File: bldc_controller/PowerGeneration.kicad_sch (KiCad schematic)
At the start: 7 parts, among them U1 MAX15062AATA+T

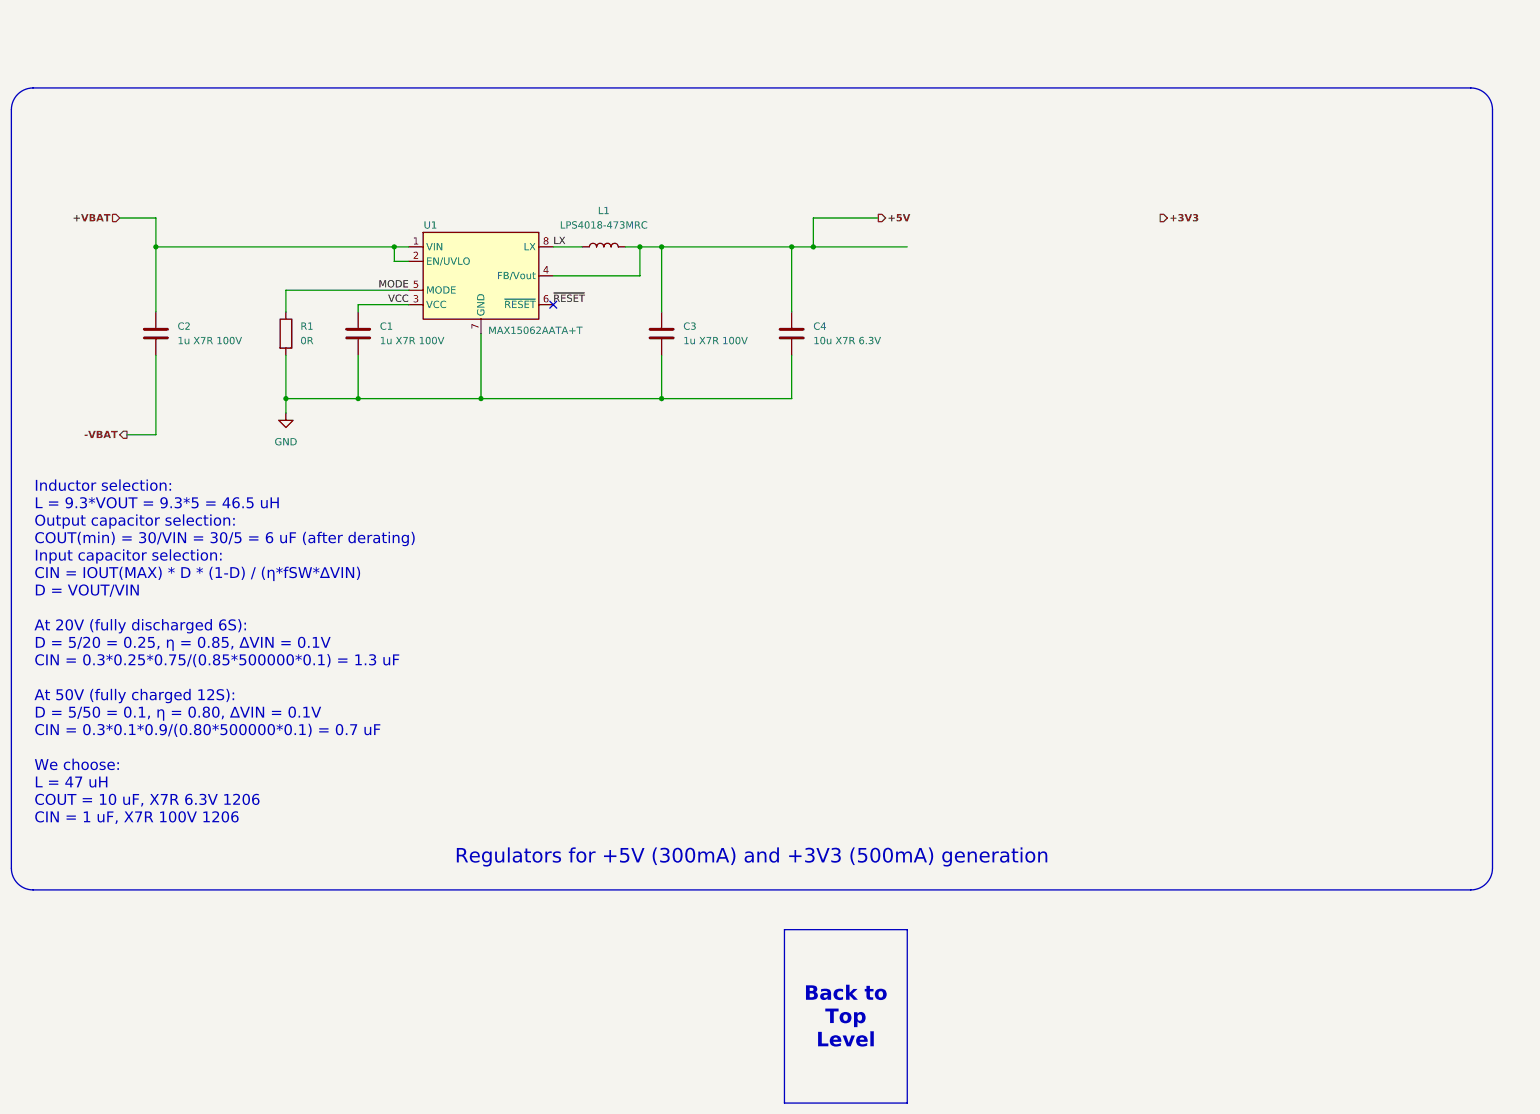
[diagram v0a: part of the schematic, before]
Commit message: added temporary footprints and deleted extra files
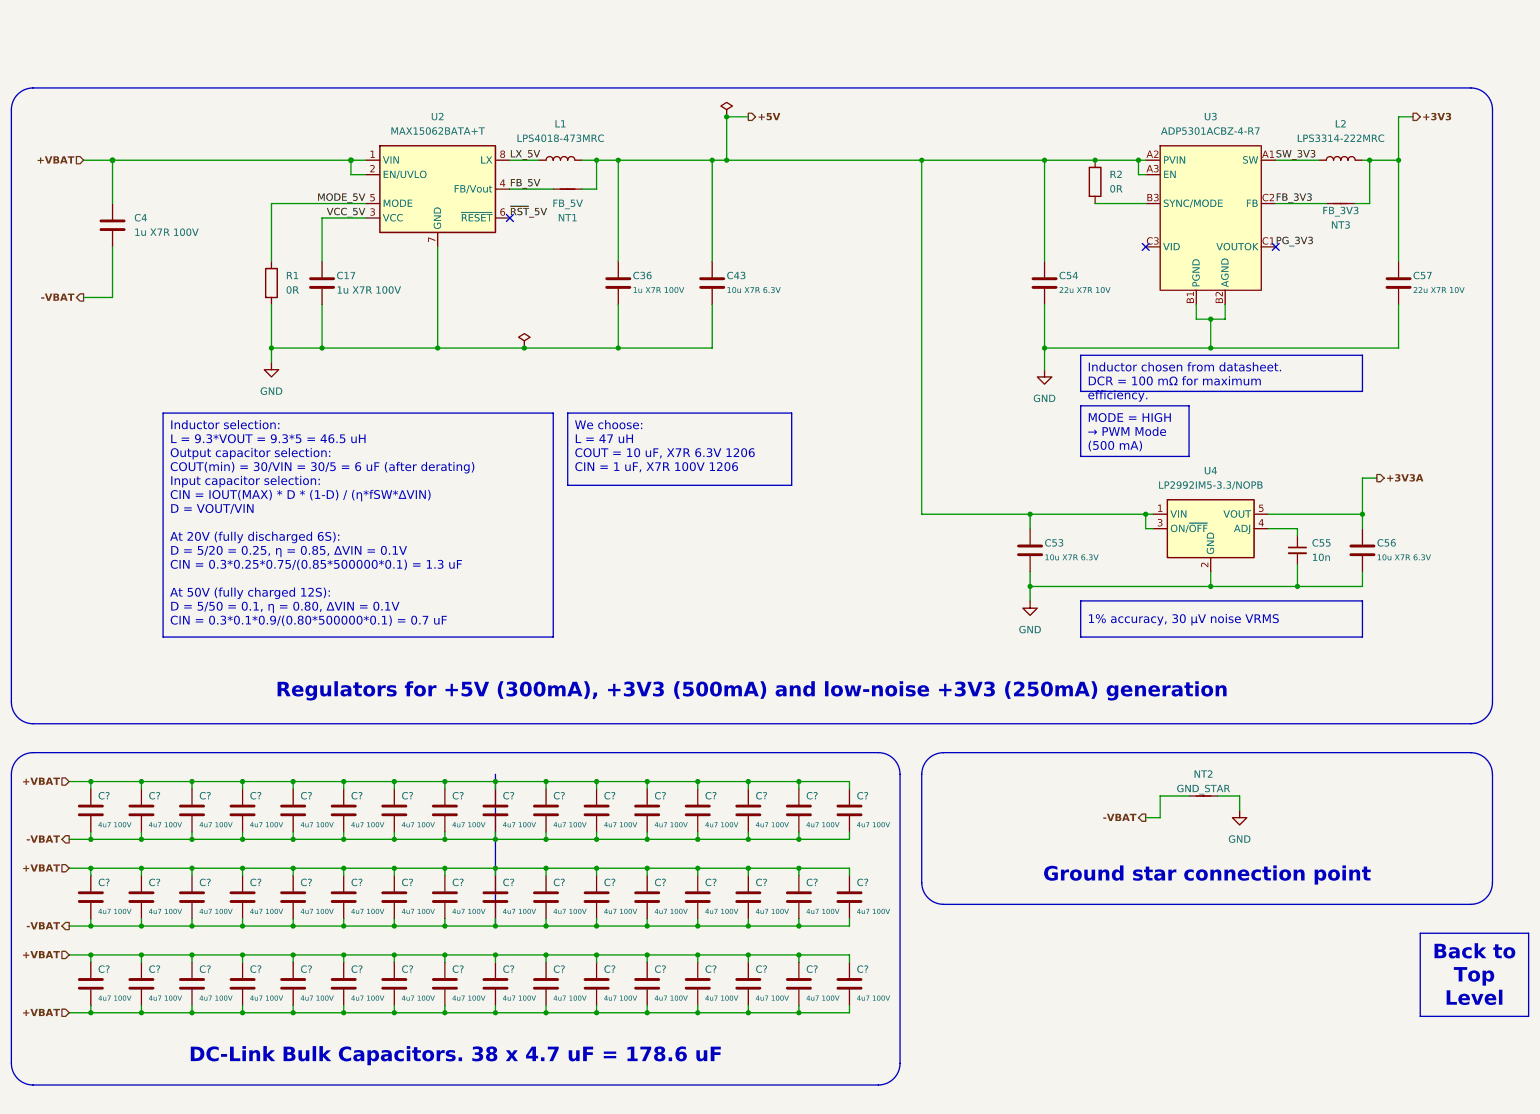
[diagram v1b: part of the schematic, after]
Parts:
- removed U1: MAX15062AATA+T, Package_DFN_QFN:DFN-8_2x2mm_P0.5mm, symbol Regulator_Switching:MAX15062A
- added C53, C56: 10u X7R 6.3V, Capacitor_SMD:C_0201_0603Metric, symbol Device:C
- added C54, C57: 22u X7R 10V, Capacitor_SMD:C_1206_3216Metric, symbol Device:C
- added C55: 10n, Capacitor_SMD:C_0402_1005Metric, symbol Device:C_Small
- added C? (x48): 4u7 100V, Capacitor_SMD:C_1206_3216Metric, symbol Device:C
- added L2: LPS3314-222MRC, Inductor_SMD:L_Coilcraft_LPS3314, symbol Device:L
- added NT1: FB_5V, NetTie:NetTie-2_SMD_Pad0.5mm, symbol Device:NetTie_2
- added NT2: GND_STAR, NetTie:NetTie-2_SMD_Pad2.0mm, symbol Device:NetTie_2
- added NT3: FB_3V3, NetTie:NetTie-2_SMD_Pad0.5mm, symbol Device:NetTie_2
- added R2: 0R, Resistor_SMD:R_0402_1005Metric, symbol Device:R
- added U2: MAX15062BATA+T, Package_DFN_QFN:DFN-8_2x2mm_P0.5mm, symbol Regulator_Switching:MAX15062B
- added U3: ADP5301ACBZ-4-R7, 0_switching_regulator:CB-9-6_ADI, symbol 0_switching_regulator:ADP5301ACBZ-4-R7
- added U4: LP2992IM5-3.3/NOPB, Package_TO_SOT_SMD:SOT-23-5, symbol 0_linear_regulator:LP2992IM5-3.3/NOPB
- C17: renamed from C1; footprint (none) -> Capacitor_SMD:C_0402_1005Metric
- C36: renamed from C3; footprint (none) -> Capacitor_SMD:C_0402_1005Metric
- C4: renamed from C2; footprint (none) -> Capacitor_SMD:C_0402_1005Metric
- C43: renamed from C4; footprint (none) -> Capacitor_SMD:C_0201_0603Metric
- R1: footprint (none) -> Resistor_SMD:R_0402_1005Metric
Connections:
- net +3V3: now also C57.1, L2.2, NT3.2
- net +5V: now also C53.1, C54.1, NT1.2, R2.1, U3.A2 (PVIN), U3.A3 (EN), U4.1 (VIN), U4.3 (ON/~{OFF})
- net +VBAT: now also C?.1, C?.1, C?.1, C?.1, C?.1, C?.1, C?.1, C?.1, C?.1, C?.1, C?.1, C?.1, C?.1, C?.1, C?.1, C?.1, C?.1, C?.1, C?.1, C?.1, C?.1, C?.1, C?.1, C?.1, C?.1, C?.1, C?.1, C?.1, C?.1, C?.1, C?.1, C?.1, C?.1, C?.1, C?.1, C?.1, C?.1, C?.1, C?.1, C?.1, C?.1, C?.1, C?.1, C?.1, C?.1, C?.1, C?.1, C?.1, C?.2, C?.2, C?.2, C?.2, C?.2, C?.2, C?.2, C?.2, C?.2, C?.2, C?.2, C?.2, C?.2, C?.2, C?.2, C?.2, U2.1 (VIN), U2.2 (EN/UVLO)
- net -VBAT: now also C?.2, C?.2, C?.2, C?.2, C?.2, C?.2, C?.2, C?.2, C?.2, C?.2, C?.2, C?.2, C?.2, C?.2, C?.2, C?.2, C?.2, C?.2, C?.2, C?.2, C?.2, C?.2, C?.2, C?.2, C?.2, C?.2, C?.2, C?.2, C?.2, C?.2, C?.2, C?.2, NT2.2
- net GND: now also C53.2, C54.2, C55.2, C56.2, C57.2, NT2.1, U2.7 (GND), U3.B1 (PGND), U3.B2 (AGND), U4.2 (GND)
- net LX renamed LX_5V
- net LX_5V: now also U2.8 (LX)
- net MODE renamed MODE_5V
- net MODE_5V: now also U2.5 (MODE)
- net VCC renamed VCC_5V
- net VCC_5V: now also U2.3 (VCC)
- new net: C55.1, U4.4 (ADJ)
- new net: R2.2, U3.B3 (SYNC/MODE)
- new net +3V3A: C56.1, U4.5 (VOUT)
- new net FB_3V3: NT3.1, U3.C2 (FB)
- new net FB_5V: NT1.1, U2.4 (FB/Vout)
- new net PG_3V3: U3.C1 (VOUTOK)
- new net SW_3V3: L2.1, U3.A1 (SW)
- new net ~{RST}_5V: U2.6 (~{RESET})
- no-connect marks 1 -> 3
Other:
- company: (none) -> EPFL Xplore
- title: (none) -> Power Generation
- moved on the sheet: C17, C36, C4, C43, L1, R1

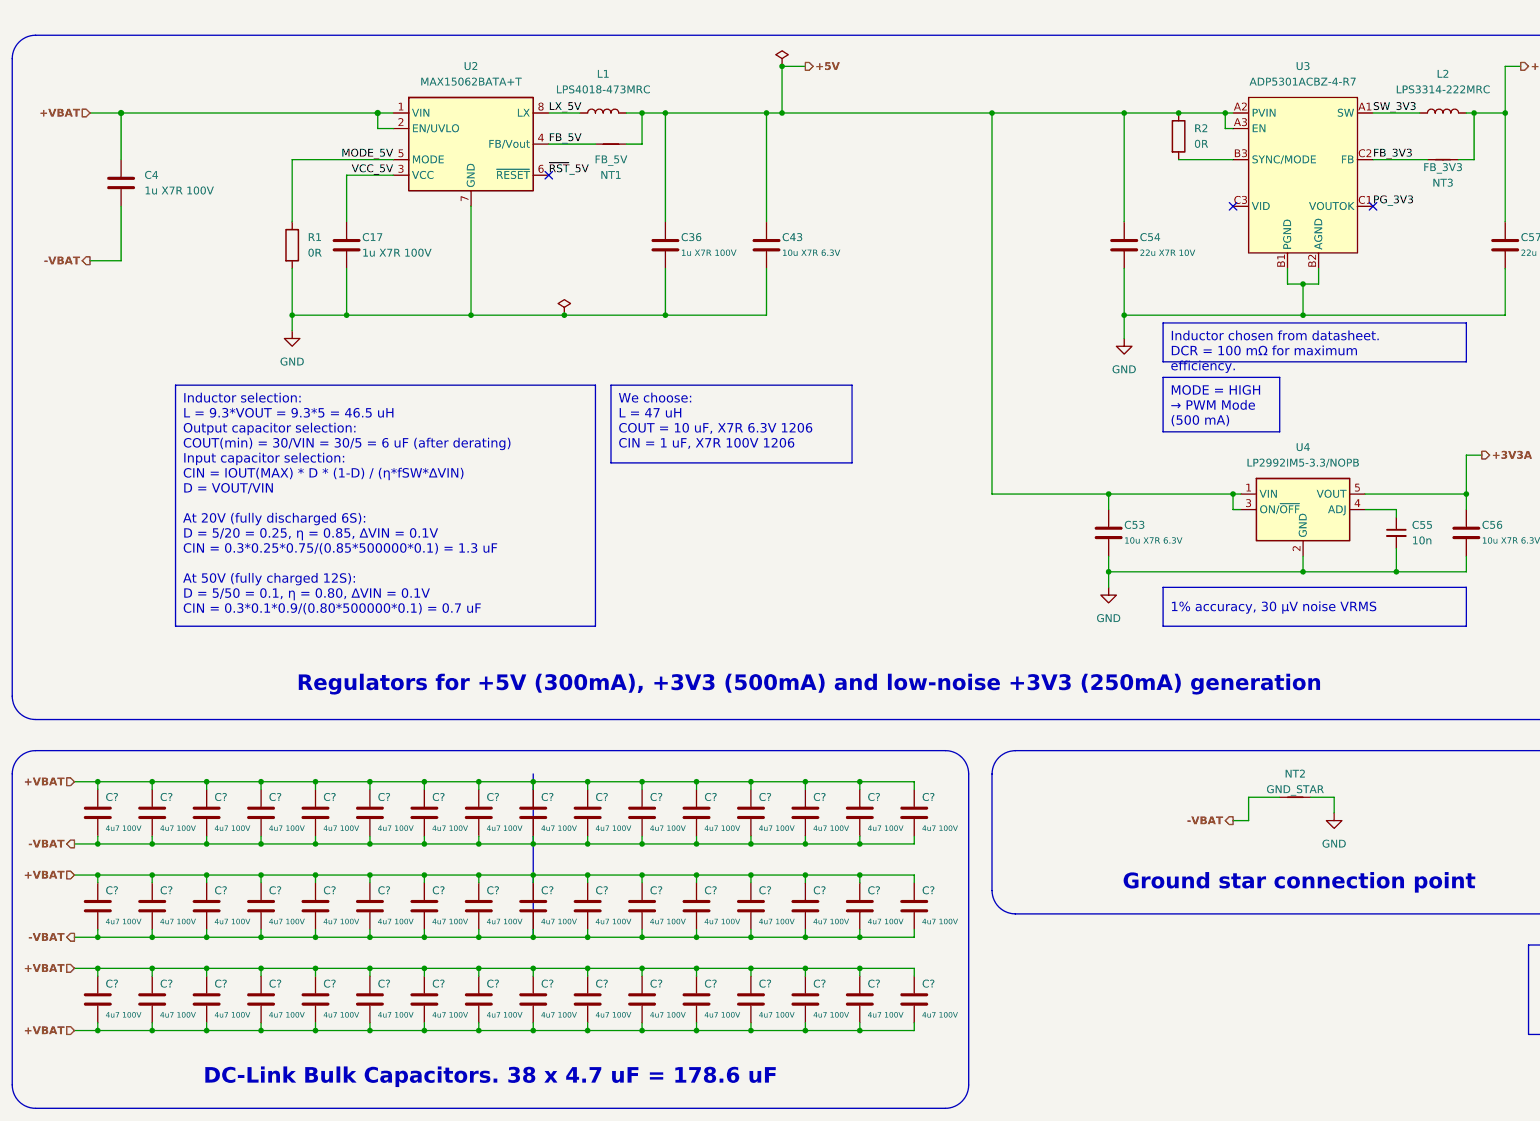
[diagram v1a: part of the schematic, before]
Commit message: added IPC-7351 compliant footprints and started routing
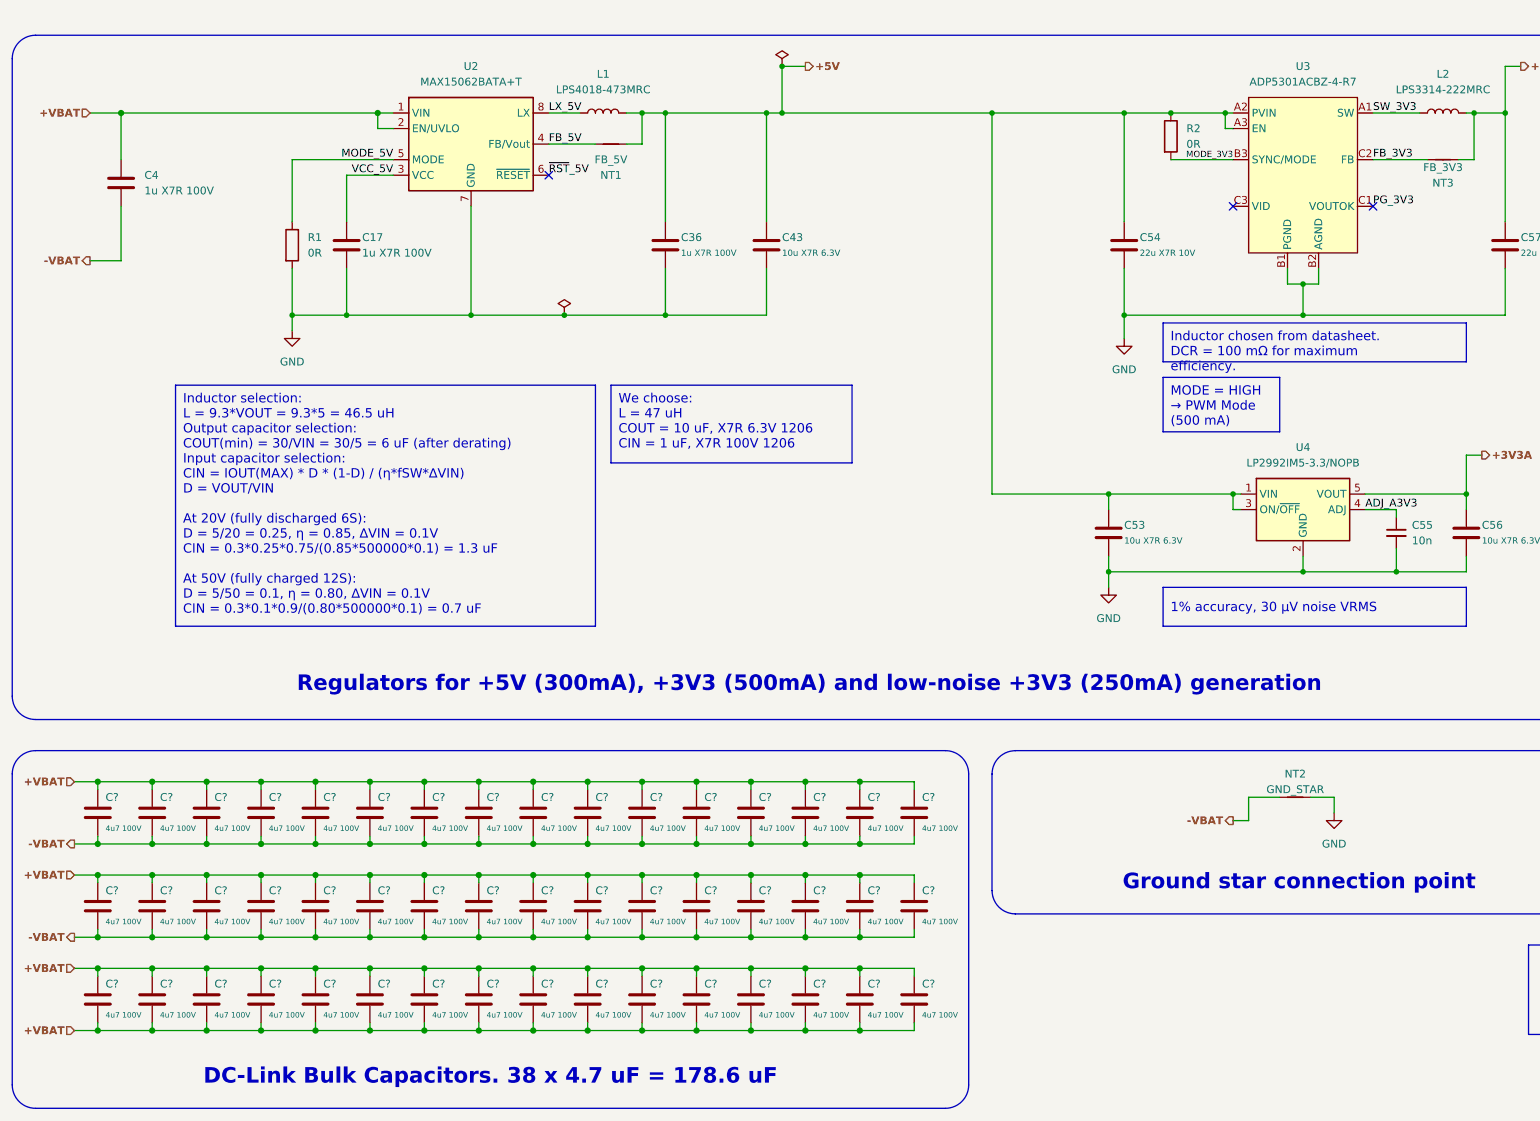
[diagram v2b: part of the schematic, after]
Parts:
- C17, C36, C4, C55: footprint Capacitor_SMD:C_0402_1005Metric -> 0_capacitor_smd:C_0402_1005_DensityHigh
- C43, C53, C56: footprint Capacitor_SMD:C_0201_0603Metric -> 0_capacitor_smd:C_0805_2012_DensityHighest
- C54, C57, C? (x48): footprint Capacitor_SMD:C_1206_3216Metric -> 0_capacitor_smd:C_1206_3216_DensityHigh
- NT1, NT3: footprint NetTie:NetTie-2_SMD_Pad0.5mm -> 0_net_tie:NetTie-2_SMD_Pad0.2mm
- R1, R2: footprint Resistor_SMD:R_0402_1005Metric -> 0_resistor_smd:R_0402_1005_DensityHigh
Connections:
- net ADJ_A3V3: now reaches C55.1, U4.4 (ADJ)
- net MODE_3V3: now reaches R2.2, U3.B3 (SYNC/MODE)
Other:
- moved on the sheet: R2
